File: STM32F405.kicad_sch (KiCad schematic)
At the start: 21 parts, among them SW1 SW_MEC_5G, U6 STM32F405RGTx, Y1 25MHz, Y2 Crystal

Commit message: precompleate PCB design
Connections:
- net Motor1_Z: now reaches U6.15 (PA1)
- net Motor1_B: now reaches U6.16 (PA2)
- net Motor1_A: now reaches U6.17 (PA3)
- net Motor2_Z: now reaches U6.23 (PA7)
- net Motor2_B: now reaches U6.26 (PB0)
- net Motor2_A: now reaches U6.27 (PB1)
- net ENABLE_1: now reaches U6.33 (PB12)
- net PWM1_left: now reaches U6.37 (PC6)
- net PWM1_right: now reaches U6.38 (PC7)
- net PWM2_left: now reaches U6.39 (PC8)
- net PWM2_right: now reaches U6.40 (PC9)
- net ENABLE_2: now reaches U6.41 (PA8)
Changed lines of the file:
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@@
+    (stroke (width 0) (type default))
+  )
+  (wire (pts (xy 168.91 128.27) (xy 171.45 128.27))
     (stroke (width 0) (type default))
   )
@@
     (stroke (width 0) (type default))
   )
+  (wire (pts (xy 168.91 74.93) (xy 171.45 74.93))
+    (stroke (width 0) (type default))
+  )
   (wire (pts (xy 63.5 54.61) (xy 74.93 54.61))
     (stroke (width 0) (type default))
@@
     (stroke (width 0) (type default))
   )
+  (wire (pts (xy 130.81 92.71) (xy 133.35 92.71))
+    (stroke (width 0) (type default))
+  )
   (wire (pts (xy 101.6 121.92) (xy 101.6 124.46))
     (stroke (width 0) (type default))
@@
     (stroke (width 0) (type default))
   )
+  (wire (pts (xy 130.81 97.79) (xy 133.35 97.79))
+    (stroke (width 0) (type default))
+  )
   (wire (pts (xy 118.11 143.51) (xy 151.13 143.51))
     (stroke (width 0) (type default))
   )
+  (wire (pts (xy 168.91 62.23) (xy 171.45 62.23))
+    (stroke (width 0) (type default))
+  )
   (wire (pts (xy 101.6 113.03) (xy 101.6 121.92))
     (stroke (width 0) (type default))
@@
     (stroke (width 0) (type default))
   )
+  (wire (pts (xy 130.81 100.33) (xy 133.35 100.33))
+    (stroke (width 0) (type default))
+  )
+  (wire (pts (xy 168.91 57.15) (xy 171.45 57.15))
+    (stroke (width 0) (type default))
+  )
   (wire (pts (xy 266.7 36.83) (xy 266.7 39.37))
     (stroke (width 0) (type default))
@@
     (stroke (width 0) (type default))
   )
+  (wire (pts (xy 168.91 72.39) (xy 171.45 72.39))
+    (stroke (width 0) (type default))
+  )
+  (wire (pts (xy 168.91 59.69) (xy 171.45 59.69))
+    (stroke (width 0) (type default))
+  )
+  (wire (pts (xy 168.91 97.79) (xy 171.45 97.79))
+    (stroke (width 0) (type default))
+  )
   (wire (pts (xy 101.6 73.66) (xy 101.6 77.47))
     (stroke (width 0) (type default))
   )
+  (wire (pts (xy 168.91 100.33) (xy 171.45 100.33))
+    (stroke (width 0) (type default))
+  )
   (wire (pts (xy 111.76 83.82) (xy 101.6 83.82))
+    (stroke (width 0) (type default))
+  )
+  (wire (pts (xy 130.81 95.25) (xy 133.35 95.25))
     (stroke (width 0) (type default))
   )
@@
     (effects (font (size 1.27 1.27)) (justify right))
   )
+  (hierarchical_label "PWM1_right" (shape output) (at 130.81 95.25 180) (fields_autoplaced)
+    (effects (font (size 1.27 1.27)) (justify right))
+  )
   (hierarchical_label "SWDIO" (shape input) (at 172.72 87.63 0) (fields_autoplaced)
     (effects (font (size 1.27 1.27)) (justify left))
   )
+  (hierarchical_label "PWM1_left" (shape output) (at 130.81 92.71 180) (fields_autoplaced)
+    (effects (font (size 1.27 1.27)) (justify right))
+  )
+  (hierarchical_label "ENABLE_2" (shape output) (at 171.45 74.93 0) (fields_autoplaced)
+    (effects (font (size 1.27 1.27)) (justify left))
+  )
+  (hierarchical_label "Motor2_B" (shape input) (at 171.45 97.79 0) (fields_autoplaced)
+    (effects (font (size 1.27 1.27)) (justify left))
+  )
+  (hierarchical_label "Motor2_A" (shape input) (at 171.45 100.33 0) (fields_autoplaced)
+    (effects (font (size 1.27 1.27)) (justify left))
+  )
+  (hierarchical_label "Motor2_Z" (shape input) (at 171.45 72.39 0) (fields_autoplaced)
+    (effects (font (size 1.27 1.27)) (justify left))
+  )
+  (hierarchical_label "ENABLE_1" (shape output) (at 171.45 128.27 0) (fields_autoplaced)
+    (effects (font (size 1.27 1.27)) (justify left))
+  )
   (hierarchical_label "3.3V_IN" (shape input) (at 148.59 36.83 90) (fields_autoplaced)
     (effects (font (size 1.27 1.27)) (justify left))
@@
     (effects (font (size 1.27 1.27)) (justify left))
   )
+  (hierarchical_label "Motor1_B" (shape input) (at 171.45 59.69 0) (fields_autoplaced)
+    (effects (font (size 1.27 1.27)) (justify left))
+  )
   (hierarchical_label "3.3V_IN" (shape input) (at 158.75 36.83 90) (fields_autoplaced)
     (effects (font (size 1.27 1.27)) (justify left))
@@
     (effects (font (size 1.27 1.27)) (justify left))
   )
+  (hierarchical_label "Motor1_A" (shape input) (at 171.45 62.23 0) (fields_autoplaced)
+    (effects (font (size 1.27 1.27)) (justify left))
+  )
   (hierarchical_label "SWO" (shape input) (at 172.72 105.41 0) (fields_autoplaced)
     (effects (font (size 1.27 1.27)) (justify left))
@@
     (effects (font (size 1.27 1.27)) (justify left))
   )
+  (hierarchical_label "PWM2_right" (shape output) (at 130.81 100.33 180) (fields_autoplaced)
+    (effects (font (size 1.27 1.27)) (justify right))
+  )
+  (hierarchical_label "PWM2_left" (shape output) (at 130.81 97.79 180) (fields_autoplaced)
+    (effects (font (size 1.27 1.27)) (justify right))
+  )
   (hierarchical_label "CAN_TX" (shape output) (at 172.72 85.09 0) (fields_autoplaced)
     (effects (font (size 1.27 1.27)) (justify left))
   )
+  (hierarchical_label "Motor1_Z" (shape input) (at 171.45 57.15 0) (fields_autoplaced)
+    (effects (font (size 1.27 1.27)) (justify left))
+  )

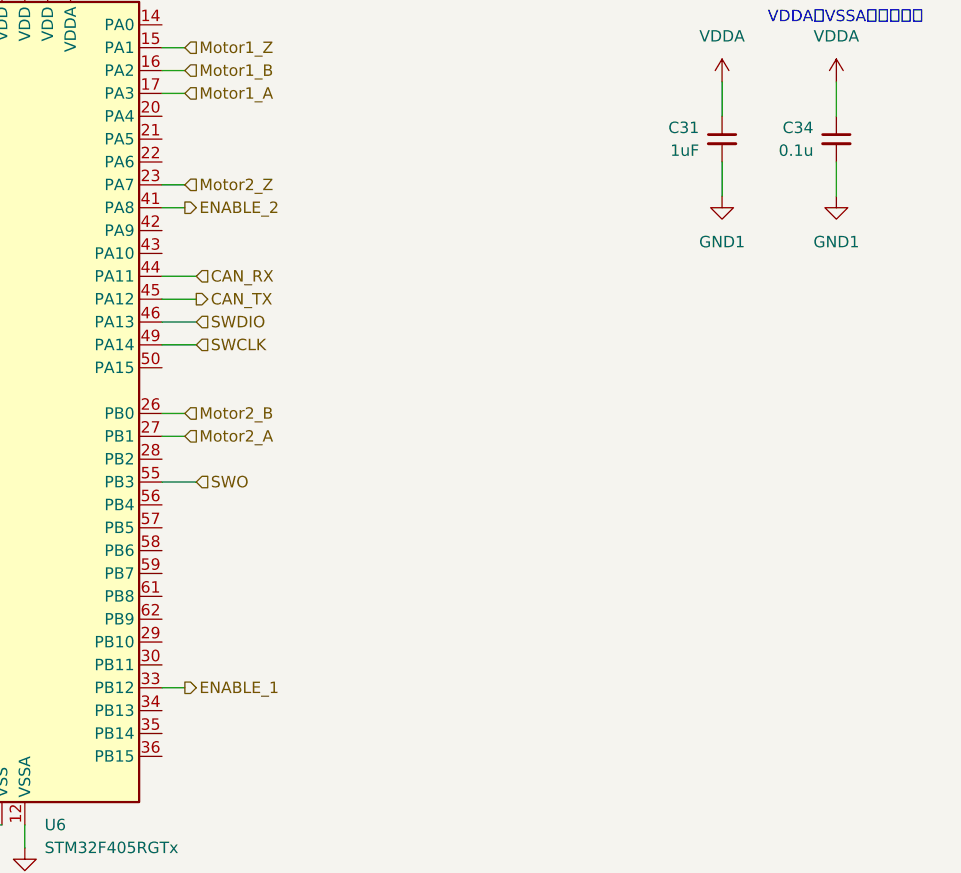
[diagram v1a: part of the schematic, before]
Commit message: add gatedriver power
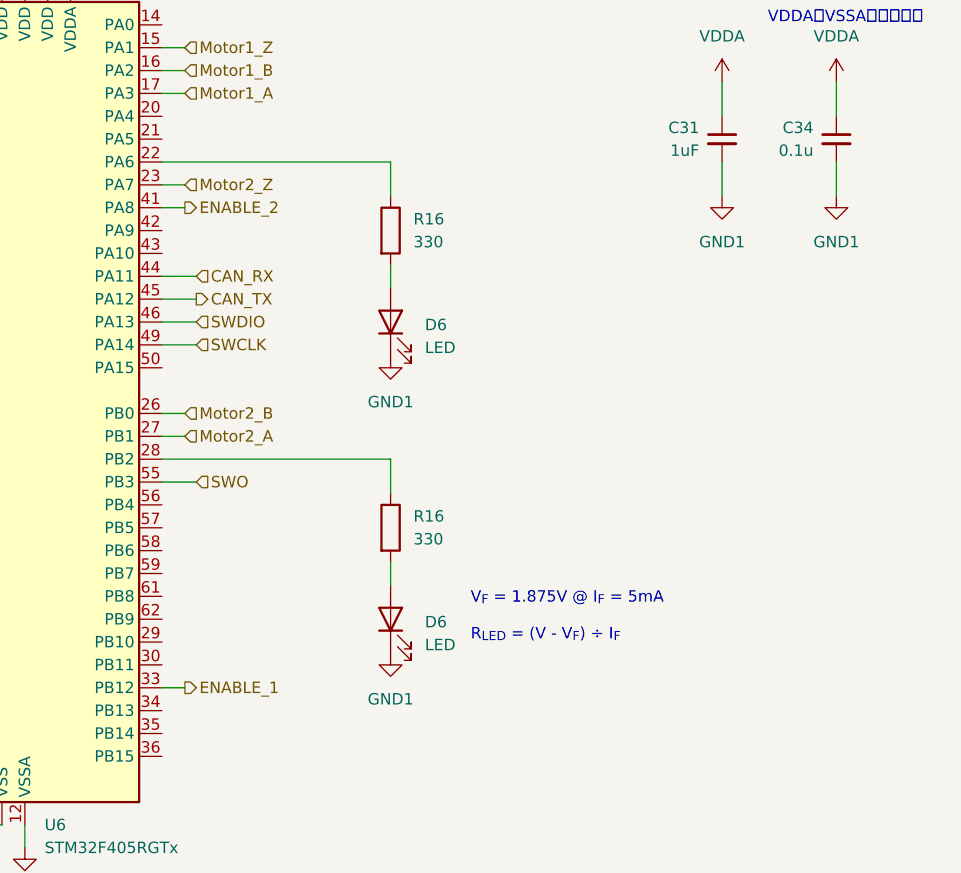
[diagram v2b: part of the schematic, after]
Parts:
- added D6 (x2): LED, LED_SMD:LED_0805_2012Metric, symbol Device:LED
- added R16 (x2): 330, Resistor_SMD:R_0603_1608Metric_Pad0.98x0.95mm_HandSolder, symbol Device:R
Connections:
- net GND1: now also D6.1 (K), D6.1 (K)
- net at U6.22 (PA6): now also R16.1
- net at U6.28 (PB2): now also R16.1
- new net: D6.2 (A), R16.2 (x2)
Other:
- note added: "V_{F} = 1.875V @ I_{F} = 5mA R_{LED} = (V - V_{F}) ÷ I_{F}"

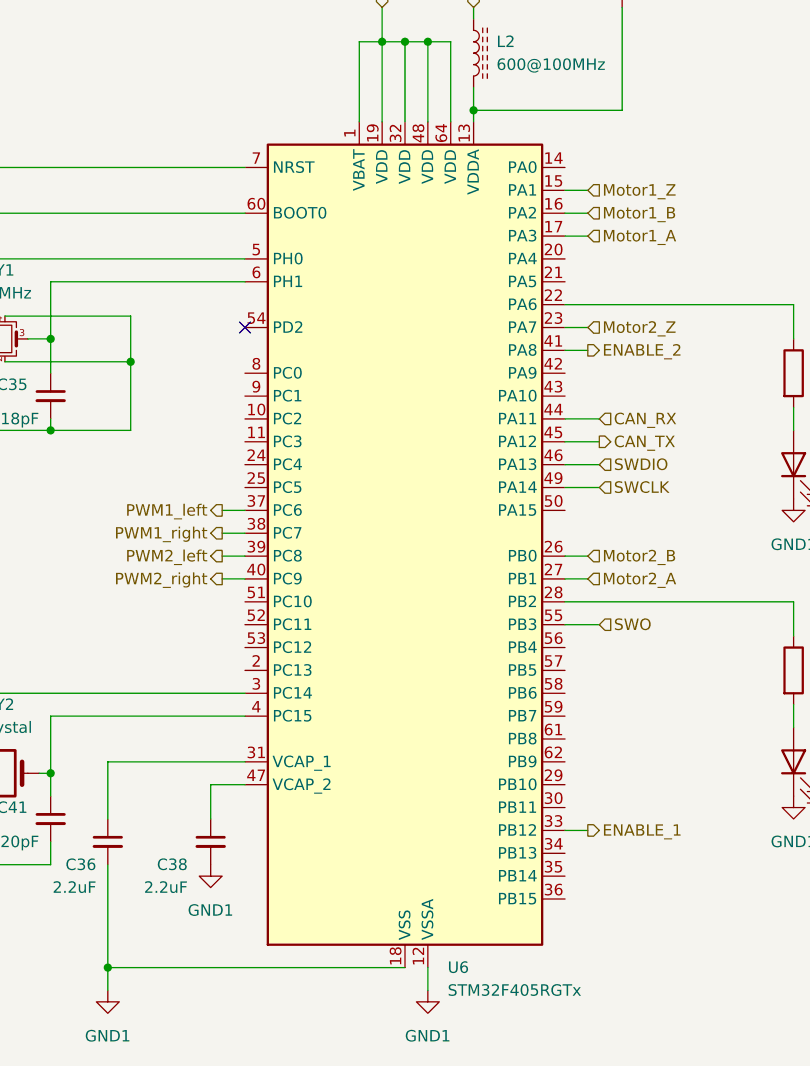
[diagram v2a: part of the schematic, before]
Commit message: add silkprint & GND plane
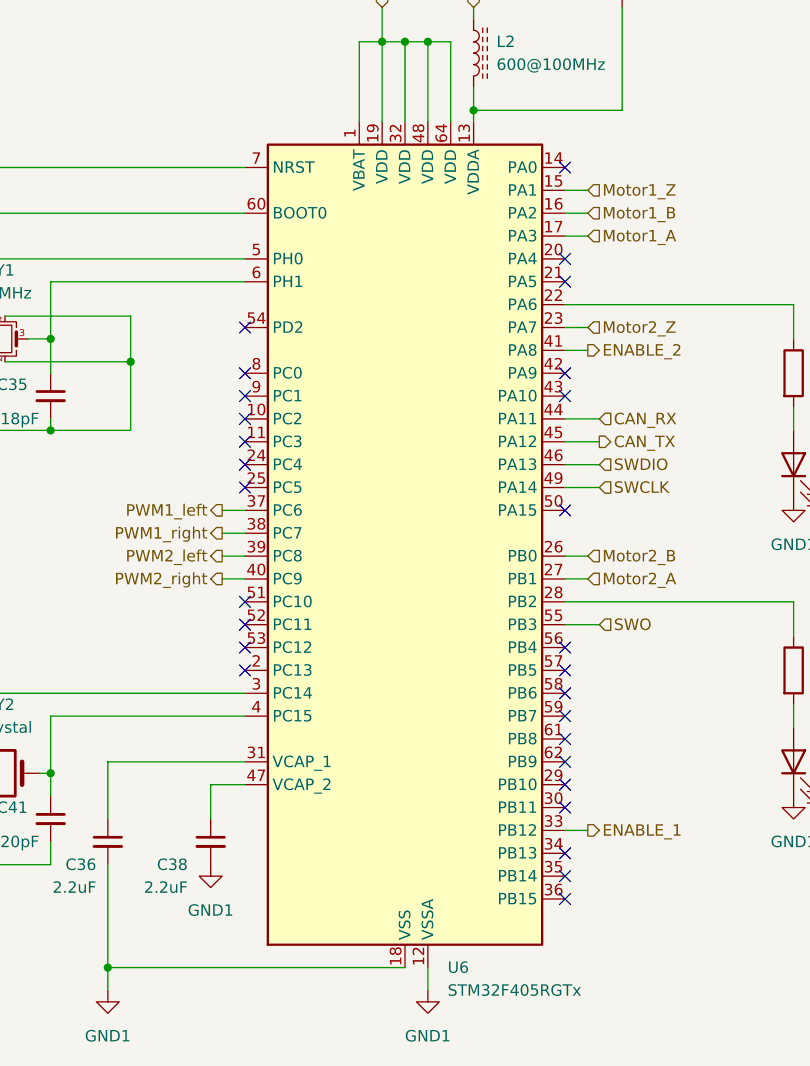
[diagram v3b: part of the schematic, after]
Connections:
- no-connect marks 1 -> 28
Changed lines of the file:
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@@
   (junction (at 111.76 73.66) (diameter 0) (color 0 0 0 0)
   )
+  (no_connect (at 133.35 80.01))
+  (no_connect (at 168.91 125.73))
+  (no_connect (at 168.91 123.19))
+  (no_connect (at 133.35 105.41))
+  (no_connect (at 168.91 107.95))
+  (no_connect (at 133.35 82.55))
+  (no_connect (at 133.35 110.49))
+  (no_connect (at 168.91 110.49))
+  (no_connect (at 133.35 107.95))
+  (no_connect (at 168.91 133.35))
+  (no_connect (at 133.35 77.47))
+  (no_connect (at 168.91 67.31))
   (no_connect (at 133.35 72.39))
+  (no_connect (at 168.91 54.61))
+  (no_connect (at 168.91 92.71))
+  (no_connect (at 133.35 90.17))
+  (no_connect (at 168.91 115.57))
+  (no_connect (at 133.35 102.87))
+  (no_connect (at 133.35 87.63))
+  (no_connect (at 168.91 64.77))
+  (no_connect (at 168.91 120.65))
+  (no_connect (at 133.35 85.09))
+  (no_connect (at 168.91 118.11))
+  (no_connect (at 168.91 130.81))
+  (no_connect (at 168.91 135.89))
+  (no_connect (at 168.91 113.03))
+  (no_connect (at 168.91 77.47))
+  (no_connect (at 168.91 80.01))
   (wire (pts (xy 146.05 49.53) (xy 146.05 40.64))
     (stroke (width 0) (type default))

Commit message: release prot.1 v0.1.0
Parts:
- added D22: LED, LED_SMD:LED_0603_1608Metric_Pad1.05x0.95mm_HandSolder, symbol Device:LED
- added R46, R47, R48, R49: 10k, Resistor_SMD:R_0402_1005Metric_Pad0.72x0.64mm_HandSolder, symbol Device:R
- added R50: 330, Resistor_SMD:R_0603_1608Metric_Pad0.98x0.95mm_HandSolder, symbol Device:R
- added SW2: SW_DIP_x04, Button_Switch_SMD:SW_DIP_SPSTx04_Slide_Copal_CHS-04B_W7.62mm_P1.27mm, symbol Switch:SW_DIP_x04
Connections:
- net 3.3V_IN: now also R50.1, SW2.5, SW2.6, SW2.7, SW2.8
- net ENABLE_1: now also U6.28 (PB2); no longer U6.33 (PB12)
- net GND1: now also D22.1 (K), R46.2, R47.2, R48.2, R49.2
- net Motor1_A: now also U6.14 (PA0); no longer U6.17 (PA3)
- net Motor1_B: now also U6.15 (PA1); no longer U6.16 (PA2)
- net Motor1_Z: now also U6.16 (PA2); no longer U6.15 (PA1)
- net Motor2_A: now also U6.22 (PA6); no longer U6.27 (PB1)
- net Motor2_B: now also U6.23 (PA7); no longer U6.26 (PB0)
- net Motor2_Z: now also U6.21 (PA5); no longer U6.23 (PA7)
- net at R16.1: now also U6.24 (PC4); no longer U6.22 (PA6)
- net at U6.25 (PC5): now also R16.1
- net at U6.34 (PB13): now also R47.1, SW2.3
- net at U6.35 (PB14): now also R48.1, SW2.2
- net at U6.36 (PB15): now also R49.1, SW2.1
- new net: D22.2 (A), R50.2
- new net: R46.1, SW2.4, U6.33 (PB12)
- no-connect marks 28 -> 24
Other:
- moved on the sheet: D6, R16

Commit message: add branch v0.2.0
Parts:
- removed C41, C42: 20pF, Capacitor_SMD:C_0402_1005Metric, symbol Device:C_Small
- removed D6: LED, LED_SMD:LED_0805_2012Metric, symbol Device:LED
- removed R16: 330, Resistor_SMD:R_0603_1608Metric_Pad0.98x0.95mm_HandSolder, symbol Device:R
- removed Y2: Crystal, Crystal:Crystal_SMD_3215-2Pin_3.2x1.5mm, symbol Device:Crystal
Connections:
- no-connect marks 24 -> 27
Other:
- moved on the sheet: D6, R16
